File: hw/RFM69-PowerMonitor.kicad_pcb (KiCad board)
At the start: 2 copper layers, 29 x 57 mm, 19 parts, among them P1 CONN_1WIRE, P2 CONN_PIR, P3 CONN_METER, P4 BNC, P5 CONN_PWR, U1 AP1117D33, U2 RFM69HW

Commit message: Final PCB design.
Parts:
- P4: value BNC -> CONN_ANT; footprint Connect:GS2 -> Connect:GS3
- moved C1 75.6 mm to (66.2, 81.5)
- moved C2 75.6 mm to (64.0, 61.5)
- moved P1 75.6 mm to (46.5, 85.8)
- moved P4 75.6 mm to (46.5, 73.7)
- moved R2 75.6 mm to (50.0, 102.2)
- moved R3 75.6 mm to (50.2, 73.3)
- moved U1 75.6 mm to (65.0, 71.5)
- moved U2 75.6 mm to (44.2, 50.3)
- moved W1 75.6 mm to (46.5, 91.0)
- moved W2 75.6 mm to (61.2, 78.3)
- moved W3 75.6 mm to (56.0, 73.3)
- moved W4 75.6 mm to (53.5, 73.3)
- moved W5 75.6 mm to (56.0, 75.8)
- moved W6 75.6 mm to (53.5, 75.8)
- moved uP1 75.6 mm to (40.8, 107.5)
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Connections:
- P4 pad 1: Net-(P4-Pad1) -> GND
- U2 pad ANT: Net-(P4-Pad1) -> Net-(P4-Pad2)
- U2 pad DIO0: Net-(U2-PadDIO0) -> (no net)
- U2 pad DIO1: Net-(U2-PadDIO1) -> (no net)
- U2 pad DIO2: Net-(U2-PadDIO2) -> (no net)
- U2 pad DIO3: Net-(U2-PadDIO3) -> (no net)
- U2 pad DIO4: Net-(U2-PadDIO4) -> (no net)
- U2 pad DIO5: Net-(U2-PadDIO5) -> (no net)
- U2 pad GNDA: Net-(P4-Pad2) -> GND
- U2 pad GNDB: Net-(U2-PadGNDB) -> GND
- U2 pad NC: Net-(U2-PadNC) -> (no net)
- uP1 pad 13: Net-(uP1-Pad13) -> (no net)
- uP1 pad 15: Net-(uP1-Pad15) -> (no net)
- uP1 pad 16: Net-(uP1-Pad16) -> (no net)
- uP1 pad 17: Net-(uP1-Pad17) -> (no net)
- uP1 pad 18: Net-(uP1-Pad18) -> Net-(U2-PadRESE)
- uP1 pad 19: Net-(uP1-Pad19) -> (no net)
- uP1 pad 20: Net-(uP1-Pad20) -> (no net)
- uP1 pad 21: Net-(U2-PadRESE) -> (no net)
- uP1 pad 23: Net-(uP1-Pad23) -> (no net)
- uP1 pad 24: Net-(uP1-Pad24) -> (no net)
- uP1 pad 25: Net-(uP1-Pad25) -> (no net)
- uP1 pad 26: Net-(uP1-Pad26) -> (no net)
- uP1 pad 7: Net-(uP1-Pad7) -> (no net)
- uP1 pad 8: Net-(uP1-Pad8) -> (no net)
- uP1 pad 9: Net-(uP1-Pad9) -> (no net)
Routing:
- net GND: track 112.3 -> 152.3 mm
- net Net-(U2-PadRESE): track 0.00 -> 29.7 mm
- net (no net): track 0.00 -> 7.90 mm
- net Net-(P4-Pad1): track 4.28 -> 0.00 mm
- net Net-(P4-Pad2): track 5.14 -> 4.01 mm
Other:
- net class RF added: clearance 0.2, trace_width 0.5, via_dia 0.6, via_drill 0.4

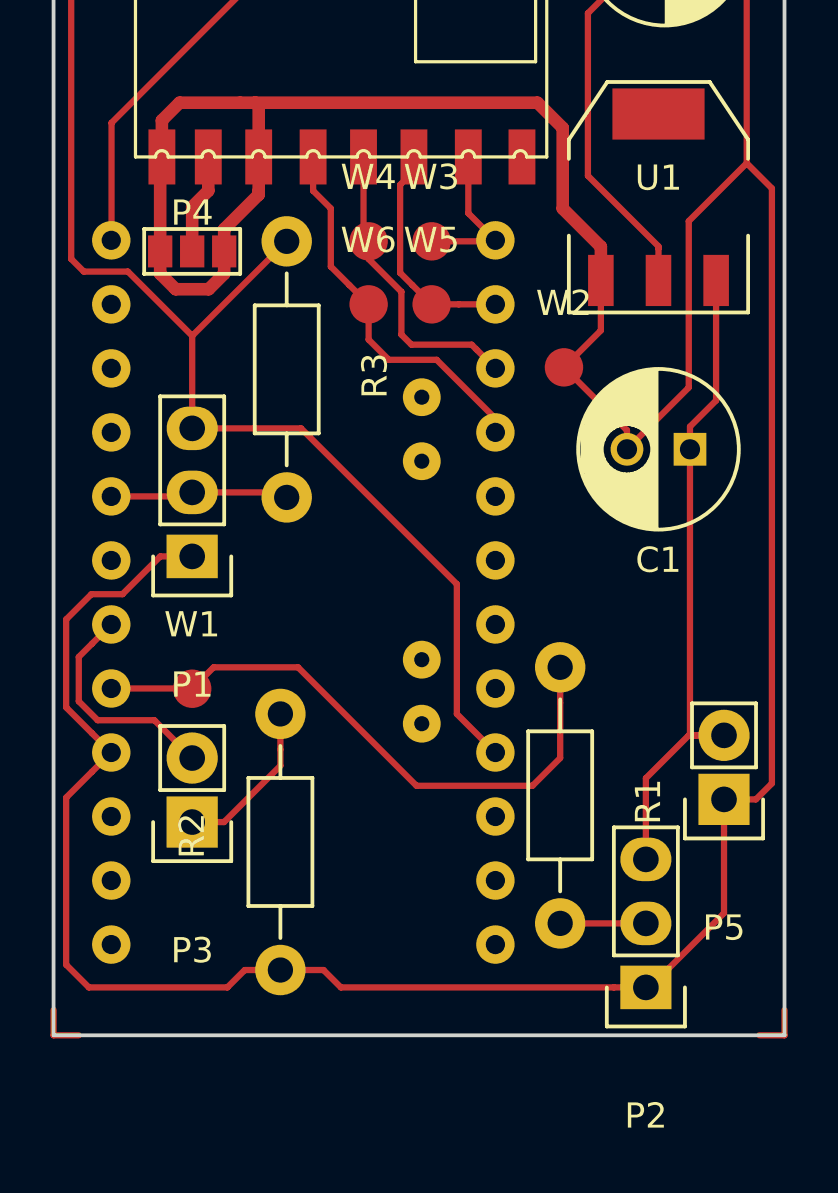
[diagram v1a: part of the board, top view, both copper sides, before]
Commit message: Removed a few PCB annotations to clean it up.
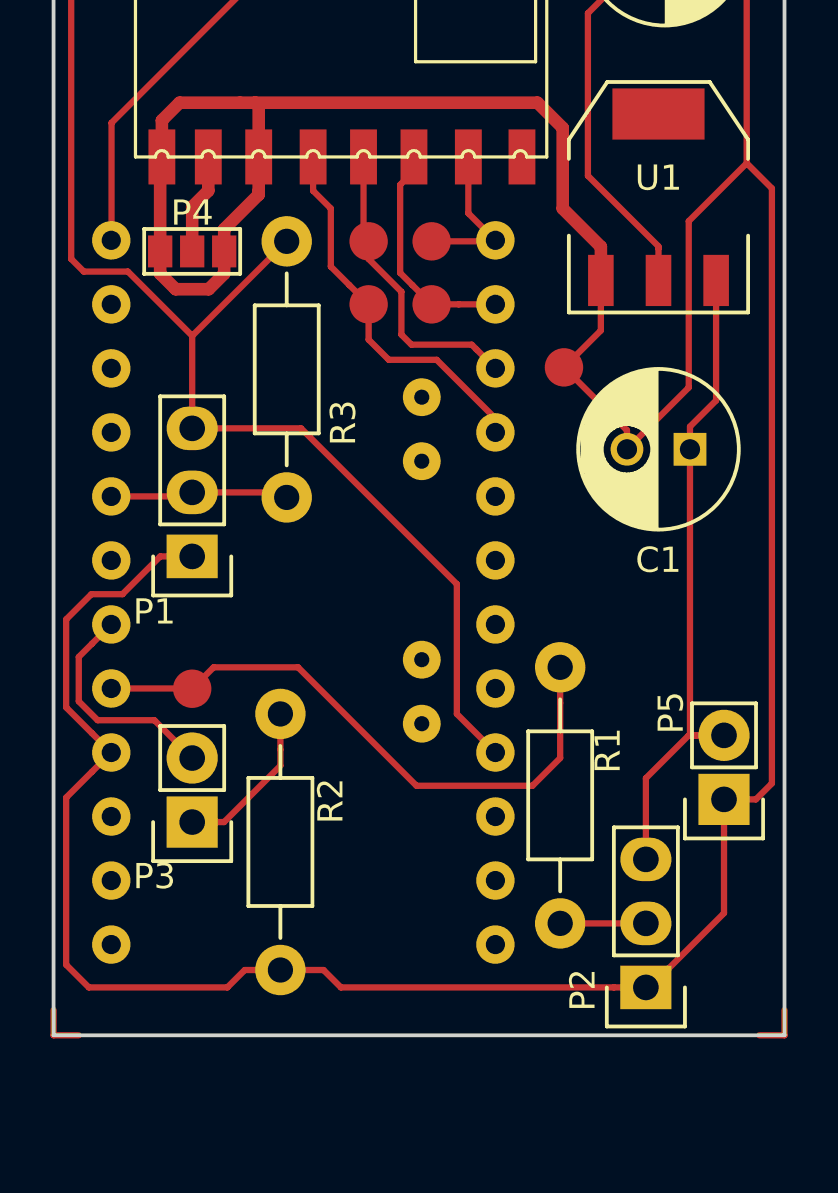
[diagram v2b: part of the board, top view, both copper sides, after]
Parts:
- ?: renamed from W4; value TEST_MISO -> (none)
- ?: renamed from W1; value TEST_PIR -> (none)
- ?: renamed from W2; value TEST_METER -> (none)
- ?: renamed from W3; value TEST_NSS -> (none)
- ?: renamed from W5; value TEST_MOSI -> (none)
- ?: renamed from W6; value TEST_SCK -> (none)
- P1: value CONN_1WIRE -> 1WIRE
- P3: value CONN_METER -> MTR
- P4: value CONN_ANT -> ANT
